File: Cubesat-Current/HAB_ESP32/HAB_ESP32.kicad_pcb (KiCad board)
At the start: 4 copper layers, 95.3 x 90.2 mm, 62 parts, among them IC1 ESP32-PICO-D4, J1 , J10 , J11 , J12 , J13 SMA_Molex_Horizontal, J2 , J3 , J4 , J5 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

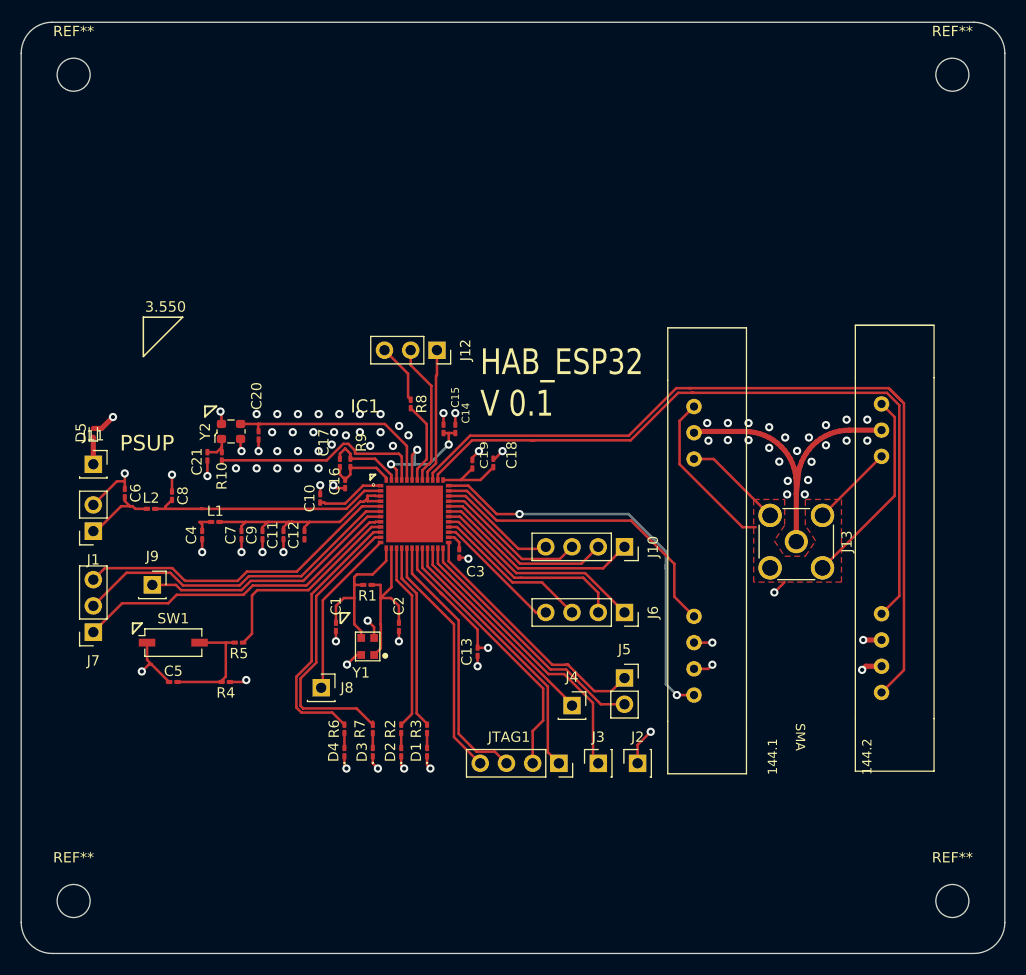
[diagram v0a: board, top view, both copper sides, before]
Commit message: Major revision to power board, three battery design v1
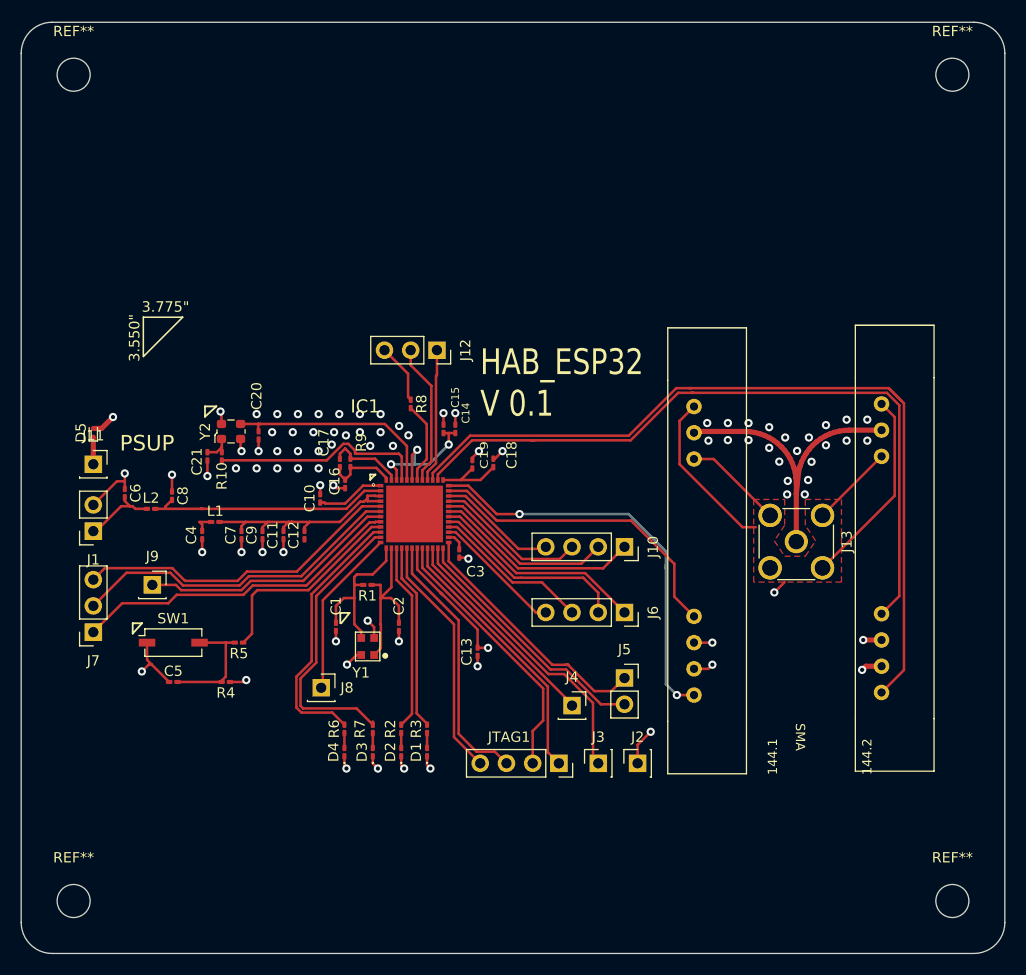
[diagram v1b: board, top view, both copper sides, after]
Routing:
- added copper zone on In1.Cu, net GND
- added copper zone on In2.Cu, net VCC
- removed copper zone on GND.Cu, net GND
- removed copper zone on PWR.Cu, net VCC
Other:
- board size 95.3 x 90.2 mm -> 95.2 x 90.2 mm
- net class Default removed
- board text added: "3.550""
- board text added: "3.775""
- board text removed: "3.550"
